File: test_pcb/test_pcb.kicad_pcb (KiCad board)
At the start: 2 copper layers, 76 x 114 mm, 87 parts, among them K0 KEYSW, K1 KEYSW, K10 KEYSW, K12 KEYSW, K13 KEYSW, K14 KEYSW, K15 KEYSW, K16 KEYSW, K17 KEYSW, K18 KEYSW, K2 KEYSW, K20 KEYSW, K21 KEYSW, K22 KEYSW, K3 KEYSW, K4 KEYSW, K5 KEYSW, K6 KEYSW, K7 KEYSW, K8 KEYSW, K9 KEYSW, P1 CONN_01X10, P10 CONN_01X01, P11 CONN_01X01, P12 CONN_01X01, P13 CONN_01X01, P14 CONN_01X01, P15 CONN_01X01, P2 CONN_01X08, P3 CONN_01X06, P4 CONN_01X01, P5 CONN_01X01, P6 CONN_01X01, P7 CONN_01X01, P8 CONN_01X01, P9 CONN_01X01, U1 STP16CP05

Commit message: test a bit better
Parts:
- moved P5 29.4 mm to (129.5, 96.2)
- moved P13 6.95 mm to (118.2, 82.5)
- moved P4 6.95 mm to (114.8, 119.8)
- moved P11 5.76 mm to (118.2, 73.8)
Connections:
- P2 pad 2: r1 -> c0
- P2 pad 3: r2 -> c1
- P2 pad 4: green1 -> c2
- P2 pad 5: c0 -> c3
- P2 pad 6: c1 -> r2
- P2 pad 7: c2 -> r1
- P2 pad 8: c3 -> green1
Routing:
- net c2: track 129.9 -> 148.6 mm, vias 5 -> 4
- net red2: track 187.3 -> 205.9 mm, vias 1 -> 2
- net green0: track 168.9 -> 150.9 mm, vias 6 -> 4
- net a3-10-0: track 35.1 -> 24.2 mm
- net r1: track 80.0 -> 70.1 mm
- net green2: track 165.9 -> 172.4 mm, vias 2 -> 3
- net a3: track 65.0 -> 58.6 mm, vias 0 -> 1
- net green1: track 163.4 -> 157.4 mm, vias 6 -> 4
- net r2: track 85.1 -> 79.4 mm
- net a3-10-1: track 25.4 -> 31.0 mm
- net Net-(JP3-Pad1): track 38.7 -> 43.6 mm, vias 0 -> 1
- net a2: track 111.0 -> 106.6 mm
- net c3: track 131.0 -> 127.2 mm, vias 2 -> 3
- net blue1: track 154.7 -> 151.0 mm, vias 7 -> 4
- net blue2: track 172.3 -> 175.7 mm, vias 6 -> 5
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
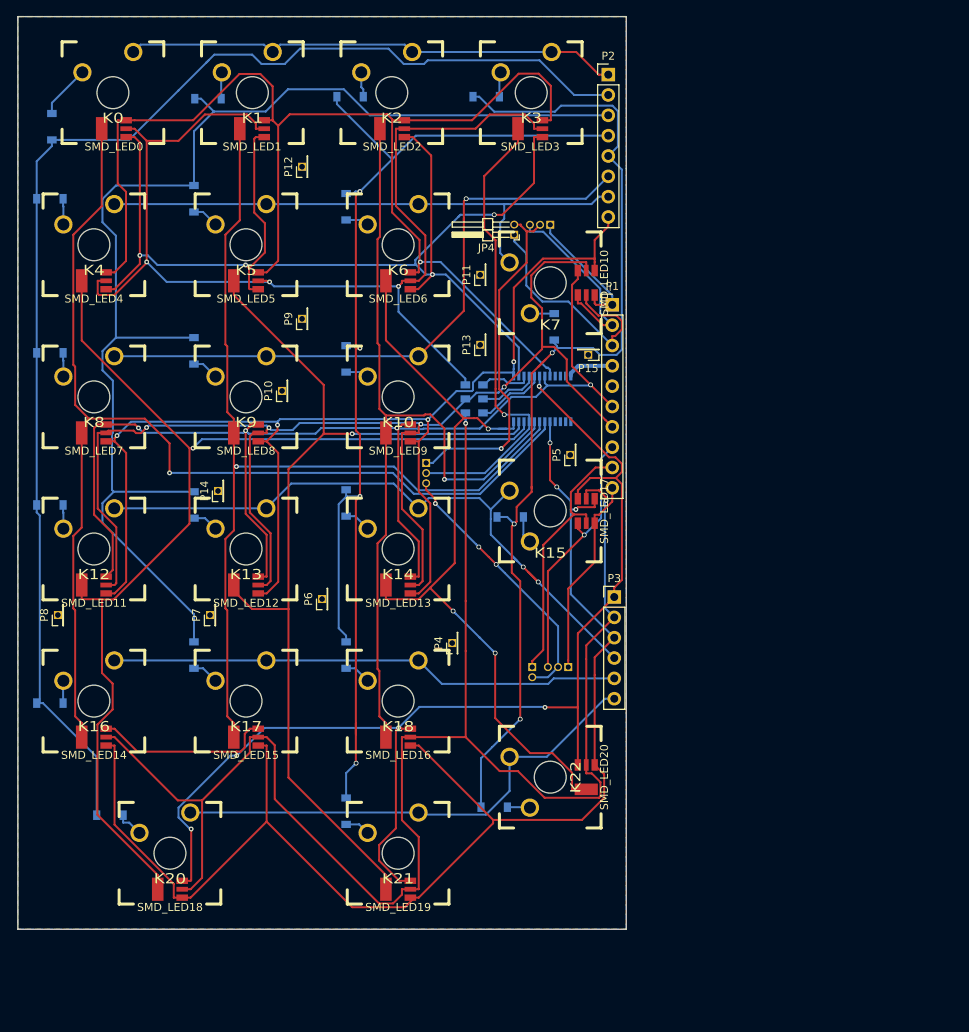
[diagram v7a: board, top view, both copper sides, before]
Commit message: test somehow improved routing adding 5 more and 1mm on the right side of the board
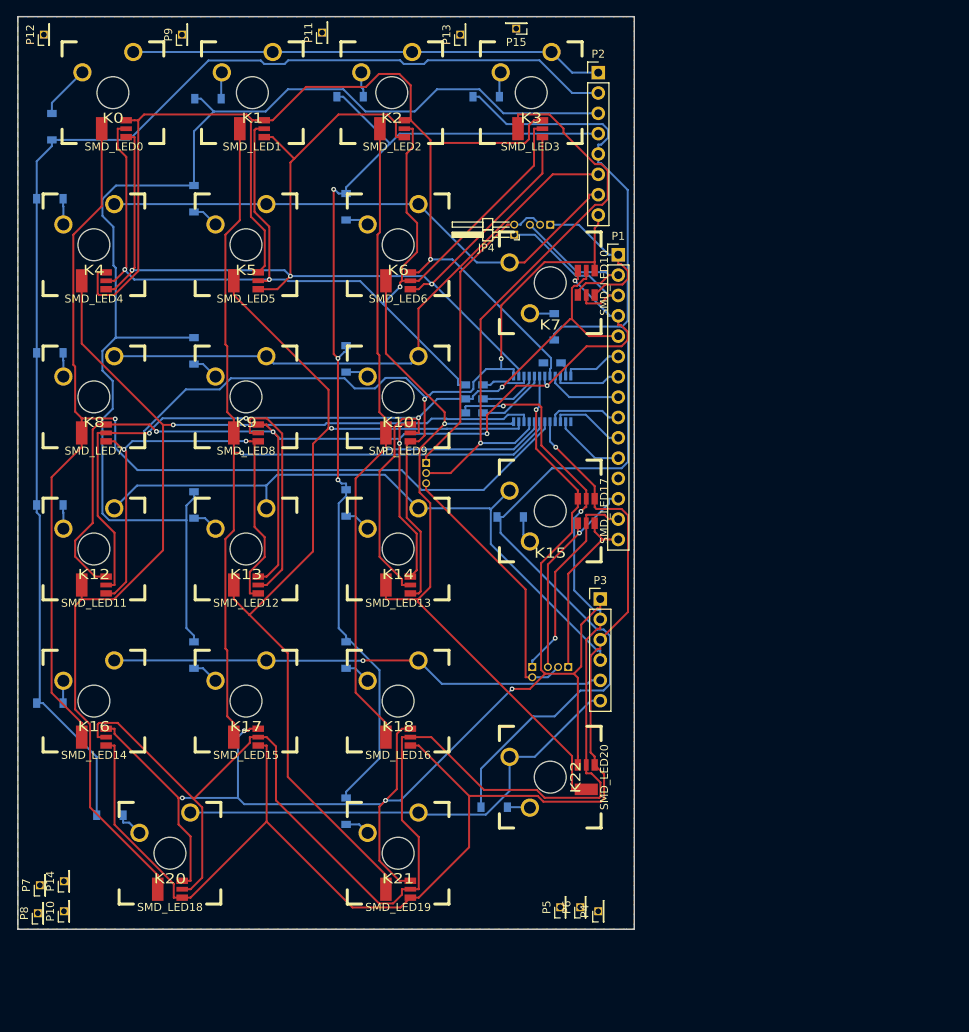
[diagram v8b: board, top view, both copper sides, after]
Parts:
- added REXT0: R, Resistors_SMD:R_0603_HandSoldering, B.Cu at (127.2, 84.8)
- P1: value CONN_01X10 -> CONN_01X15; footprint Socket_Strips:Socket_Strip_Straight_1x10_Pitch2.54mm -> Socket_Strips:Socket_Strip_Straight_1x15_Pitch2.54mm
- moved P10 70.5 mm to (66.2, 153.2)
- moved P5 56.5 mm to (128.2, 152.8)
- moved P14 52.4 mm to (66.2, 149.5)
- moved P6 50.2 mm to (130.8, 152.8)
- moved P15 41.7 mm to (122.8, 43.0)
- moved P7 39.9 mm to (63.2, 150.0)
- moved P13 38.8 mm to (115.8, 43.8)
- moved P9 38.5 mm to (81.0, 43.8)
- moved P4 38.1 mm to (133.0, 153.2)
- moved P8 37.3 mm to (63.0, 153.5)
- moved P12 36.2 mm to (63.8, 43.8)
- moved P11 36.1 mm to (98.5, 43.5)
- moved P1 6.29 mm to (135.5, 71.2)
- moved P3 1.77 mm to (133.2, 114.2)
- moved P2 1.27 mm to (133.0, 48.5)
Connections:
- P1 pad 10: a3-17-2 -> CLK
- P1 pad 4: +3V3 -> blue1
- P1 pad 5: GND -> red1
- P1 pad 6: blue1 -> +3V3
- P1 pad 7: red1 -> SDO
- P1 pad 8: a3-17-0 -> OE
- P1 pad 9: a3-17-1 -> LE
- U1 pad 2: (no net) -> SDI
- U1 pad 21: (no net) -> OE
- U1 pad 22: (no net) -> SDO
- U1 pad 23: (no net) -> Net-(REXT0-Pad2)
- U1 pad 3: (no net) -> CLK
- U1 pad 4: (no net) -> LE
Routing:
- net c2: track 148.6 -> 129.7 mm, vias 4 -> 3
- net c3: track 127.2 -> 144.3 mm, vias 3 -> 0
- net green1: track 157.4 -> 173.1 mm
- net a3: track 58.6 -> 73.4 mm
- net red2: track 205.9 -> 191.4 mm
- net OE: track 0.00 -> 9.48 mm
- net a3-10-1: track 31.0 -> 21.6 mm
- net CLK: track 0.00 -> 9.30 mm
- net LE: track 0.00 -> 9.29 mm
- net SDI: track 0.00 -> 8.97 mm
- net SDO: track 0.00 -> 8.43 mm
- net a3-17-1: track 33.2 -> 26.1 mm, vias 0 -> 1
- net red0: track 140.1 -> 147.0 mm
- net a2: track 106.6 -> 100.3 mm
- net a3-17-0: track 32.6 -> 26.7 mm
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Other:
- board size 76 x 114 mm -> 77 x 114 mm
